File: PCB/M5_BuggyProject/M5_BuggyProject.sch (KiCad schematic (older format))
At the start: 26 parts, among them J1 XT60, J2 VCC, J3 10V, J4 Receiver

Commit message: Moved config LEDs, added OSH logo.
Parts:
- removed H5: MountingHole, symbol Mechanical:MountingHole
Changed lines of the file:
@@
 	1    0    0    -1
 $EndComp
+Text GLabel 2450 4250 2    50   Input ~ 0
+CONFIG_L
 Text GLabel 2450 4150 2    50   Input ~ 0
-CONFIG_L
-Text GLabel 2450 4250 2    50   Input ~ 0
 CONFIG_R
 Text GLabel 1450 3650 0    50   Input ~ 0
@@
 	0    -1   -1   0
 $EndComp
-$Comp
-L Mechanical:MountingHole H5
-U 1 1 620461DC
-P 6700 4250
-F 0 "H5" H 6800 4296 50  0000 L CNN
-F 1 "MountingHole" H 6800 4205 50  0000 L CNN
-F 2 "" H 6700 4250 50  0001 C CNN
-F 3 "~" H 6700 4250 50  0001 C CNN
-	1    6700 4250
-	1    0    0    -1
-$EndComp
 $EndSCHEMATC

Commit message: Started PCB v2
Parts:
- removed D2, D4: ORANGE, LED_SMD:LED_1206_3216Metric, symbol Device:LED
- removed J2: VCC, TestPoint:TestPoint_Loop_D1.80mm_Drill1.0mm_Beaded, symbol Connector:Conn_01x01_Male
- removed J3: 10V, TestPoint:TestPoint_Loop_D1.80mm_Drill1.0mm_Beaded, symbol Connector:Conn_01x01_Male
- removed R2, R3: 100, Resistor_SMD:R_1206_3216Metric, symbol Device:R
- added J2: VCC, TestPoint:TestPoint_Plated_Hole_D5.0mm, symbol Connector_Generic:Conn_01x01
- added J3: 10V, TestPoint:TestPoint_Plated_Hole_D5.0mm, symbol Connector_Generic:Conn_01x01
- added J5: GND, TestPoint:TestPoint_Plated_Hole_D5.0mm, symbol Connector_Generic:Conn_01x01
- added J6: AIN1, Connector_PinSocket_2.54mm:PinSocket_1x02_P2.54mm_Vertical, symbol Connector_Generic:Conn_01x02
- added J7: AIN2, Connector_PinSocket_2.54mm:PinSocket_1x02_P2.54mm_Vertical, symbol Connector_Generic:Conn_01x02
- added J8: BIN1, Connector_PinSocket_2.54mm:PinSocket_1x02_P2.54mm_Vertical, symbol Connector_Generic:Conn_01x02
- added J9: BIN2, Connector_PinSocket_2.54mm:PinSocket_1x02_P2.54mm_Vertical, symbol Connector_Generic:Conn_01x02
- H1, H2, H3, H4: footprint MountingHole:MountingHole_3.2mm_M3_Pad_Via -> MountingHole:MountingHole_4.3mm_M4_Pad_Via
- Z1: value Diode -> Zener
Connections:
- net +10V: now also J3.1 (Pin_1)
- net AIN1: now also J6.2 (Pin_2)
- net AIN2: now also J7.2 (Pin_2)
- net BIN1: now also J8.2 (Pin_2)
- net BIN2: now also J9.2 (Pin_2)
- net GND: now also J5.1 (Pin_1), J6.1 (Pin_1), J7.1 (Pin_1), J8.1 (Pin_1), J9.1 (Pin_1); no longer H1.1, H2.1, H3.1, H4.1
- net VCC: now also J2.1 (Pin_1)
- net CONFIG_L: no longer names the net of A1.10 (A7)
- net CONFIG_R: no longer names the net of A1.9 (A6)
- no-connect marks 15 -> 21
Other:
- note added: "MCU Connections + Testpoints"
- note removed: "MCU Connections"
- moved on the sheet: A1, A2, A3, A4, A5, A6, A7, BZ1, C1, D1, D3, H1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

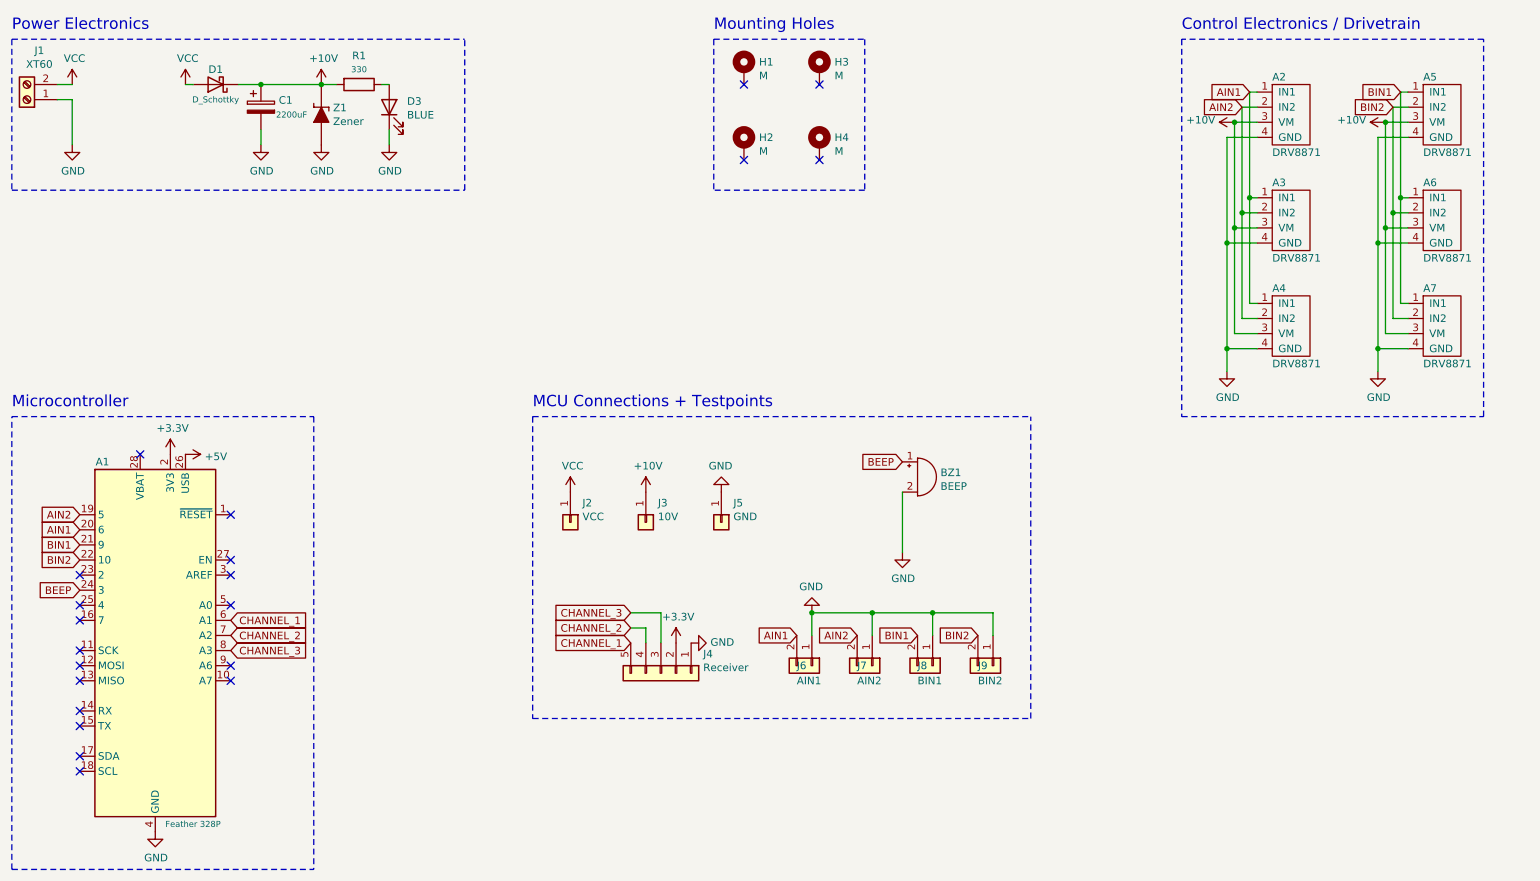
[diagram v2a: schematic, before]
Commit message: Added UMass logo, moved things around
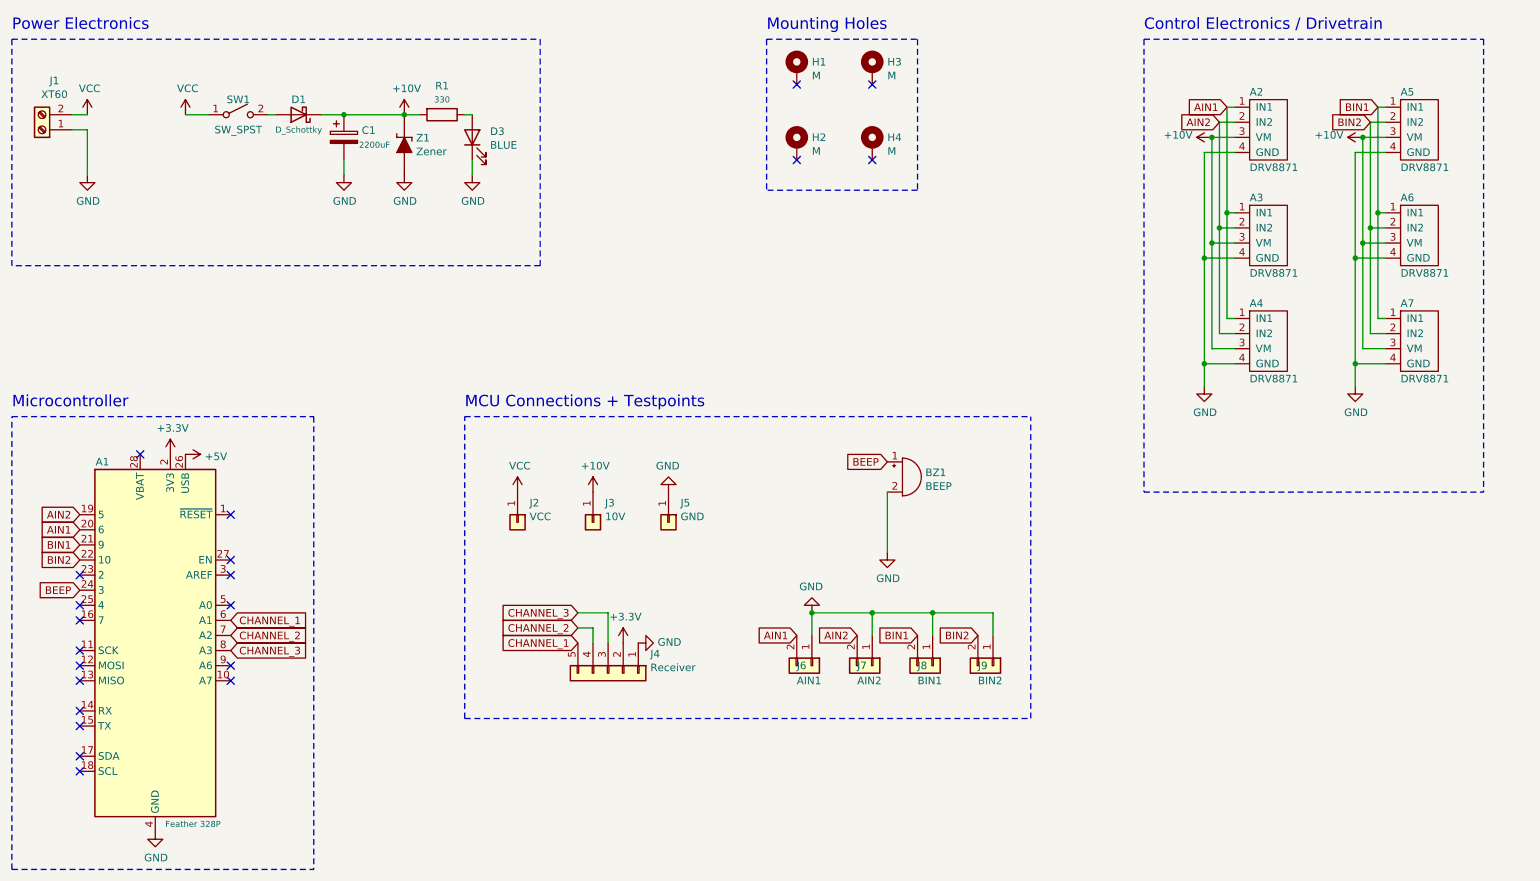
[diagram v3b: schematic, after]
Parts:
- added SW1: SW_SPST, symbol Switch:SW_SPST
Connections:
- net VCC: now also SW1.1 (A); no longer D1.2 (A)
- new net: D1.2 (A), SW1.2 (B)
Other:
- moved on the sheet: A2, A3, A4, A5, A6, A7, BZ1, C1, D1, D3, H1, H2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

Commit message: Updated PCB
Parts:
- removed J2: VCC, TestPoint:TestPoint_Plated_Hole_D5.0mm, symbol Connector_Generic:Conn_01x01
- removed SW1: SW_SPST, symbol Switch:SW_SPST
- added SW1: SW_SPDT, Buggy_Footprints:1101M2S3CQE2, symbol Switch:SW_SPDT
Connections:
- net VCC: now also SW1.1 (A)
- net at D1.2 (A): now also SW1.2 (B)
- no-connect marks 21 -> 22
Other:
- moved on the sheet: A2, A3, A4, A5, A6, A7, BZ1, J3, J4, J5, J6, J7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
